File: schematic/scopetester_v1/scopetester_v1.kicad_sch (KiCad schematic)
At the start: 40 parts, among them J1 CON_PWR, J2 CON_OUT, J3 AVR_ISP, J4 CON_GND, SW1 SW_Push, U1 ATmega8A-P, Y1 12MHz

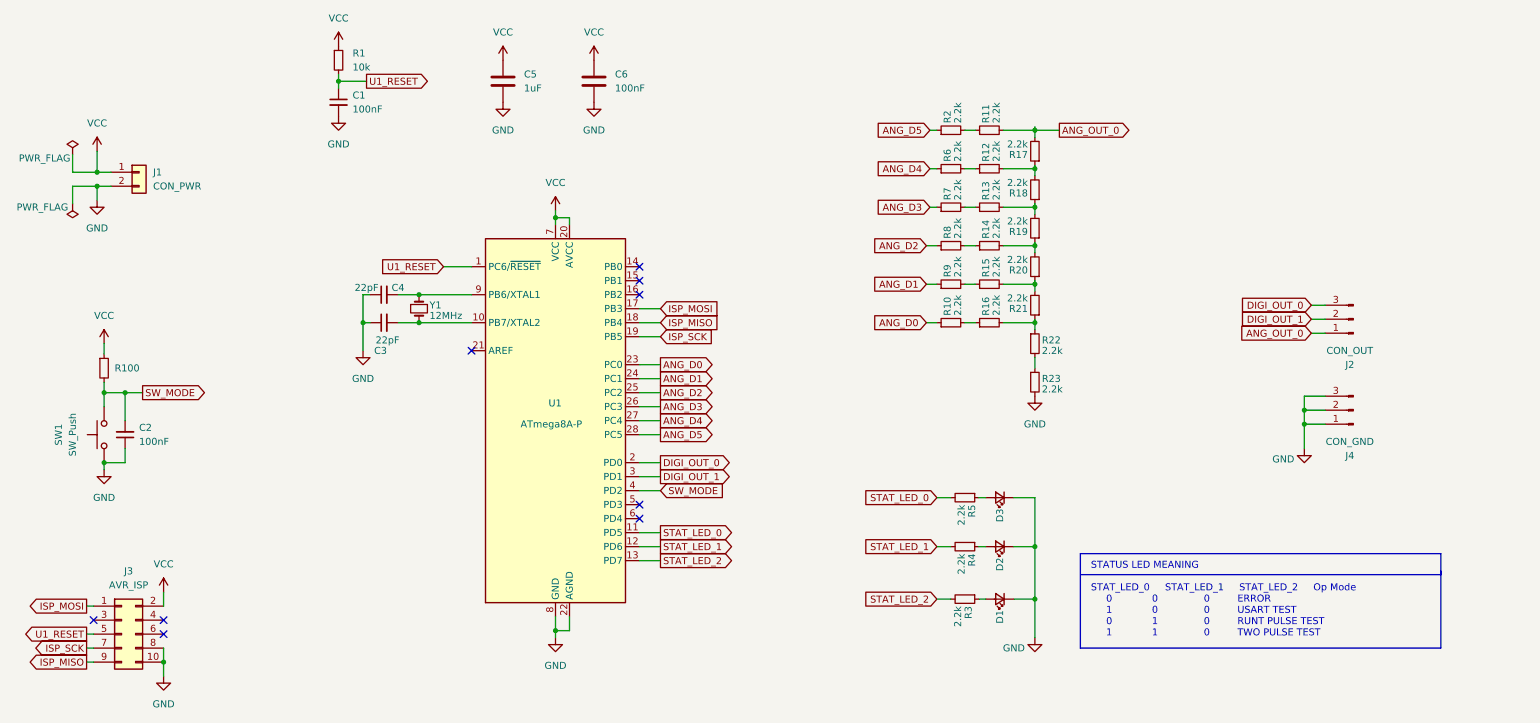
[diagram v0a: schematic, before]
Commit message: Minor updates, makes DAC clear & change of title
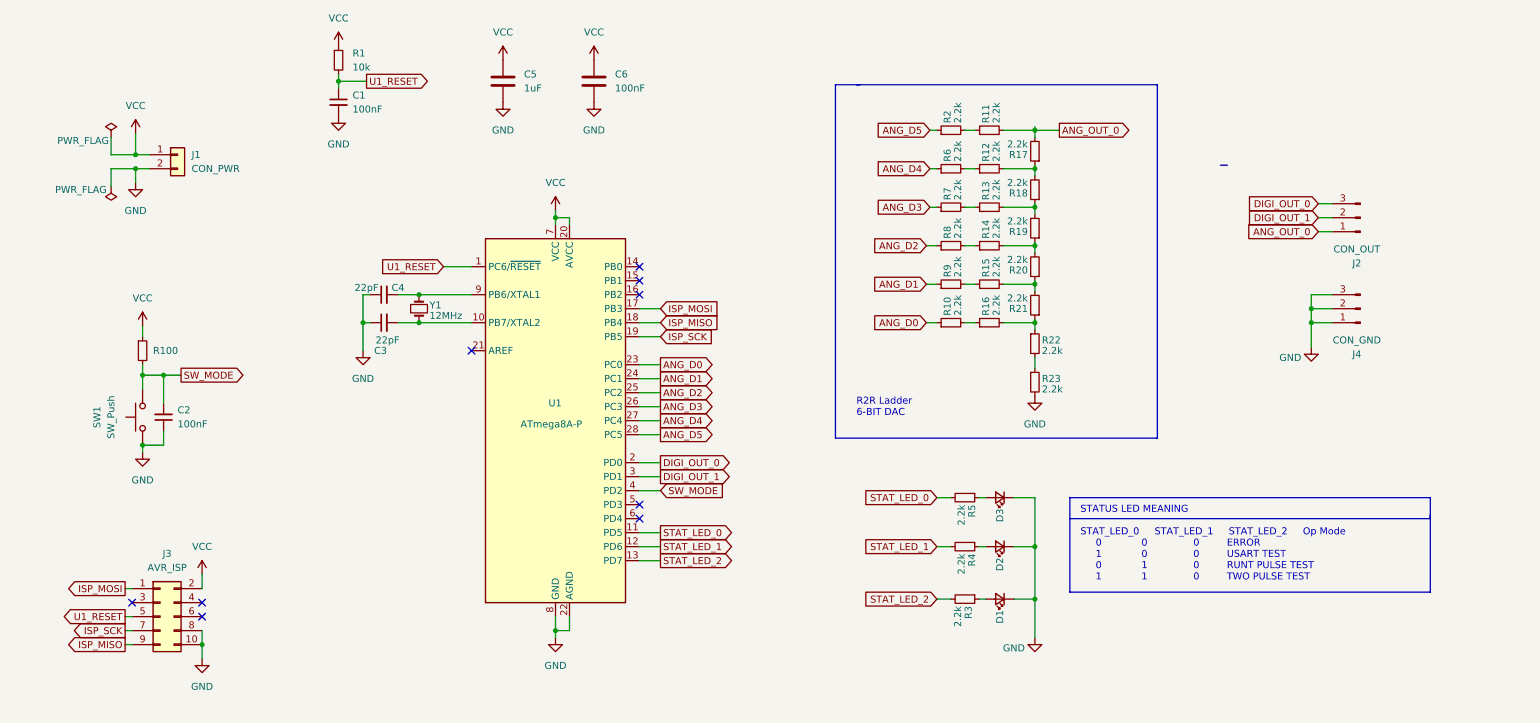
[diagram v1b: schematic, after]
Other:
- note added: "R2R Ladder 6-BIT DAC"
- moved on the sheet: C2, J1, J2, J3, J4, R100, SW1

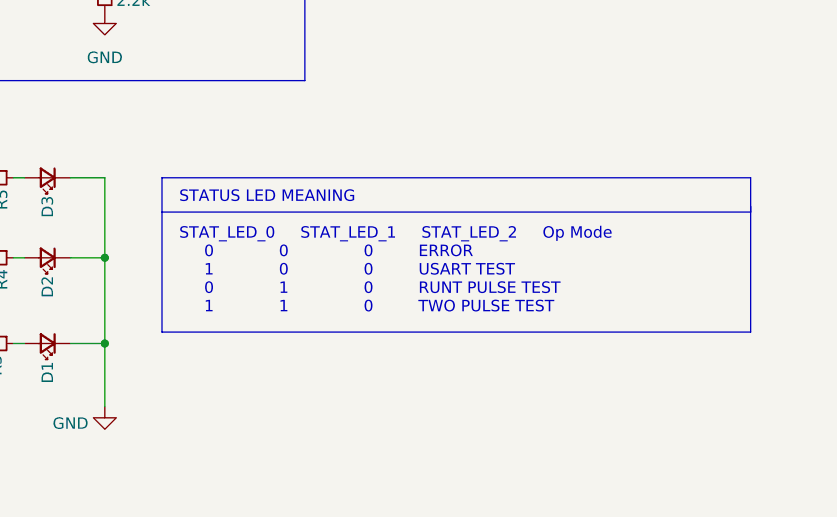
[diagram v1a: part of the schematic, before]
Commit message: Modes updated in schematic & initial PCB layout
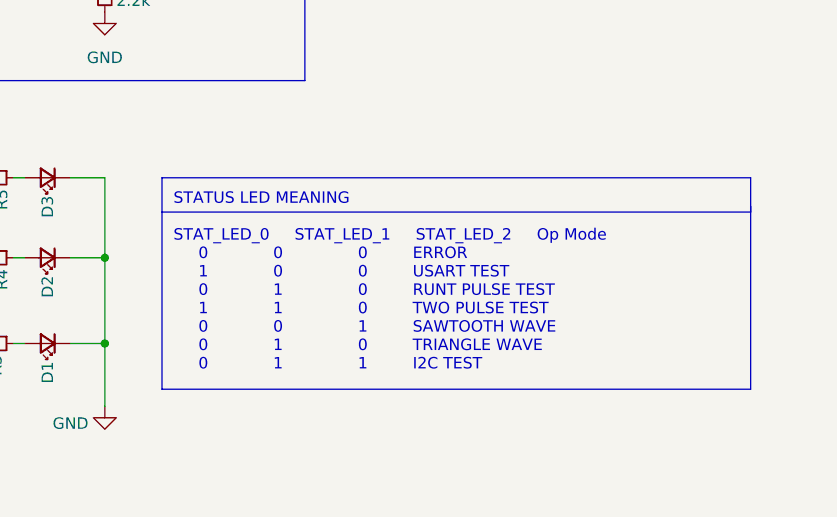
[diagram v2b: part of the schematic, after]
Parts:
- C1, C2, C3, C4, C6: footprint (none) -> Capacitor_THT:C_Disc_D3.4mm_W2.1mm_P2.50mm
- C5: footprint (none) -> Capacitor_THT:CP_Radial_D4.0mm_P1.50mm
- D1, D2, D3: footprint (none) -> LED_THT:LED_D3.0mm
- J1: footprint (none) -> Connector_PinHeader_1.00mm:PinHeader_1x02_P1.00mm_Vertical
- J2, J4: footprint (none) -> Connector_PinHeader_1.00mm:PinHeader_1x03_P1.00mm_Vertical
- J3: footprint (none) -> Connector_PinHeader_1.00mm:PinHeader_2x05_P1.00mm_Vertical
- R1, R10, R100, R11, R12, R13, R14, R15, R16, R17, R18, R19, R2, R20, R21, R22, R23, R3, R4, R5, R6, R7, R8, R9: footprint (none) -> Resistor_THT:R_Axial_DIN0411_L9.9mm_D3.6mm_P5.08mm_Vertical
- SW1: footprint (none) -> Button_Switch_THT:SW_PUSH_6mm_H5mm
- Y1: footprint (none) -> Crystal:Crystal_HC18-U_Vertical
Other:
- note added: "STATUS LED MEANING STAT_LED_0 STAT_LED_1 STAT_LED_2 Op Mode 0 0 0 ERROR 1 0 0 USART TEST 0 1 0 RUNT PULSE TEST 1 1 0 TWO PULSE TEST 0 0 1 SAWTOOTH WAVE 0 1 0 TRIANGLE WAVE 0 1 1 I2C TEST"
- note removed: "STATUS LED MEANING STAT_LED_0 STAT_LED_1 STAT_LED_2 Op Mode 0 0 0 ERROR 1 0 0 USART TEST 0 1 0 RUNT PULSE TEST 1 1 0 TWO PULSE TEST"

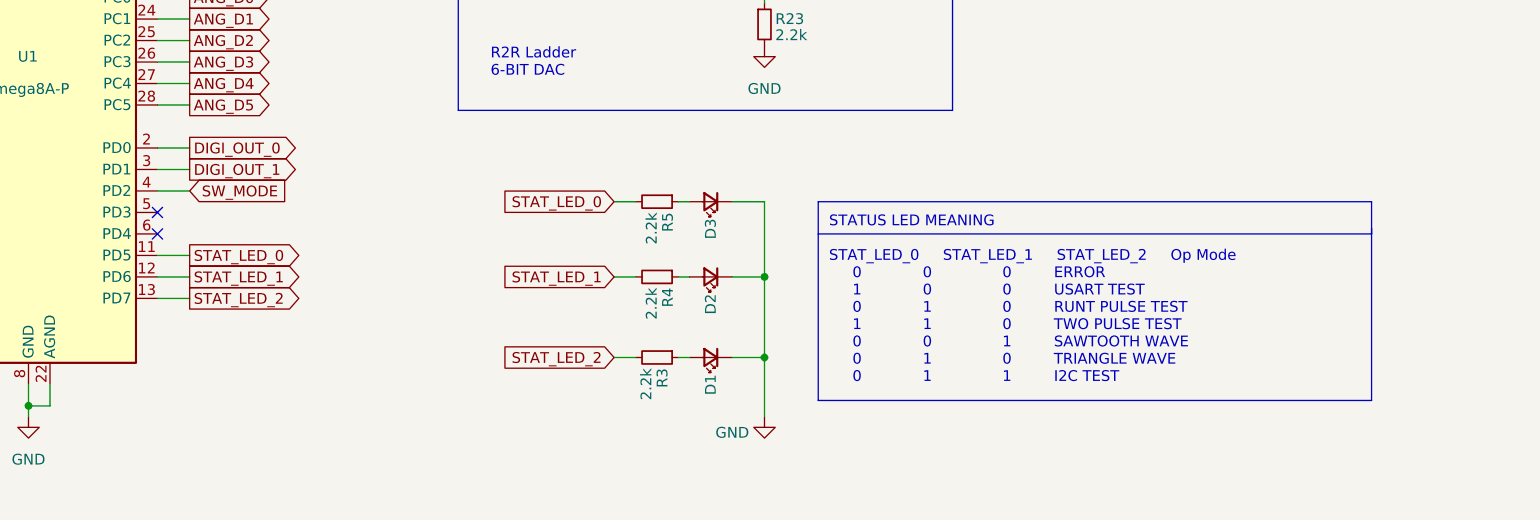
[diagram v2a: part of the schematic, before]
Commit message: There are now 4 status LEDs instead of 3
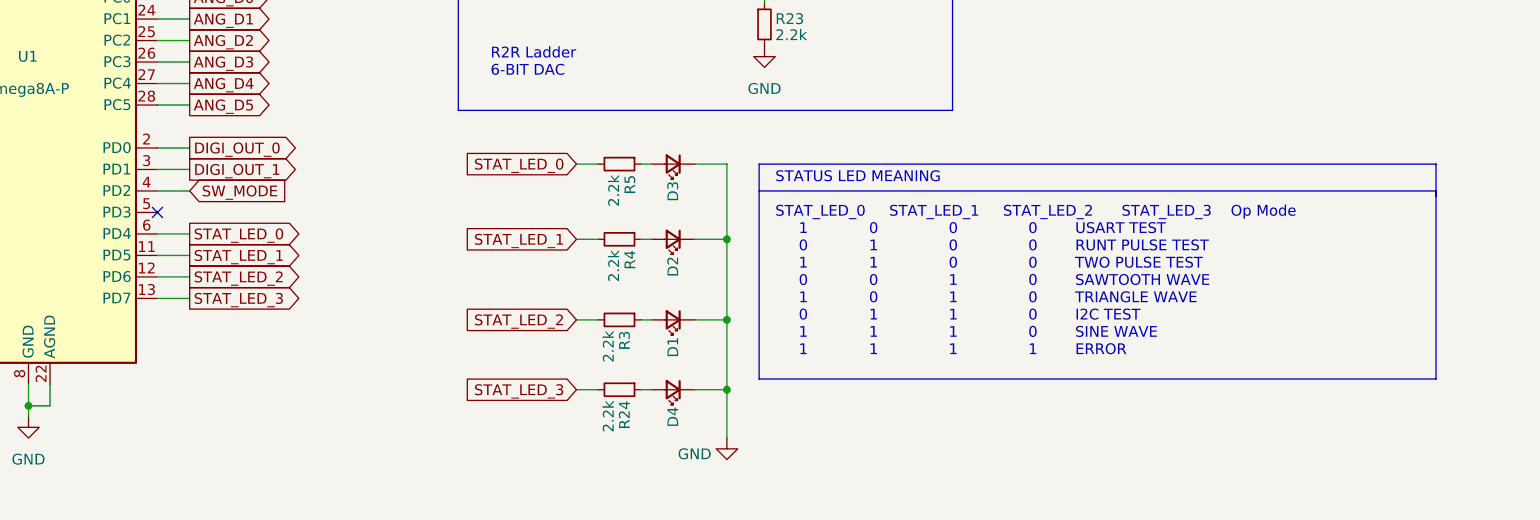
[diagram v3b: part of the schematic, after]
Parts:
- added D4: LED_Small, LED_THT:LED_D3.0mm, symbol Device:LED_Small
- added R24: 2.2k, Resistor_THT:R_Axial_DIN0411_L9.9mm_D3.6mm_P5.08mm_Vertical, symbol Device:R_Small
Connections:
- net GND: now also D4.1 (K)
- net STAT_LED_0: now also U1.6 (PD4); no longer U1.11 (PD5)
- net STAT_LED_1: now also U1.11 (PD5); no longer U1.12 (PD6)
- net STAT_LED_2: now also U1.12 (PD6); no longer U1.13 (PD7)
- new net: D4.2 (A), R24.1
- new net STAT_LED_3: R24.2, U1.13 (PD7)
- no-connect marks 9 -> 8
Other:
- note added: "STATUS LED MEANING STAT_LED_0 STAT_LED_1 STAT_LED_2 STAT_LED_3 Op Mode 1 0 0 0 USART TEST 0 1 0 0 RUNT PULSE TEST 1 1 0 0 TWO PULSE TEST 0 0 1 0 SAWTOOTH WAVE 1 0 1 0 TRIANGLE WAVE 0 1 1 0 I2C TEST 1 1 1 0 SINE WAVE 1 1 1 1 ERROR"
- note removed: "STATUS LED MEANING STAT_LED_0 STAT_LED_1 STAT_LED_2 Op Mode 0 0 0 ERROR 1 0 0 USART TEST 0 1 0 RUNT PULSE TEST 1 1 0 TWO PULSE TEST 0 0 1 SAWTOOTH WAVE 0 1 0 TRIANGLE WAVE 0 1 1 I2C TEST"
- moved on the sheet: D1, D2, D3, R3, R4, R5

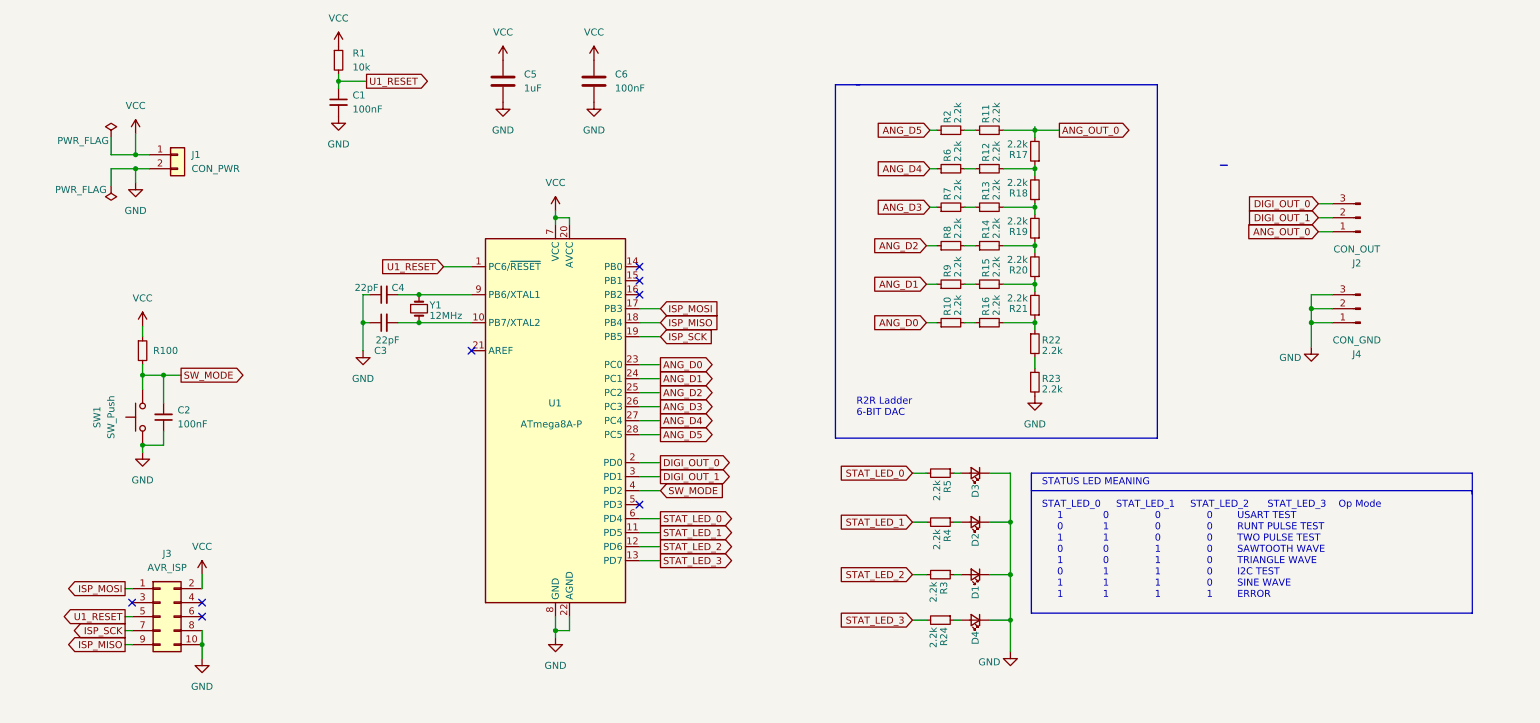
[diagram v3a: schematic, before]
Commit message: Replaced Vcc with +5V in schematic
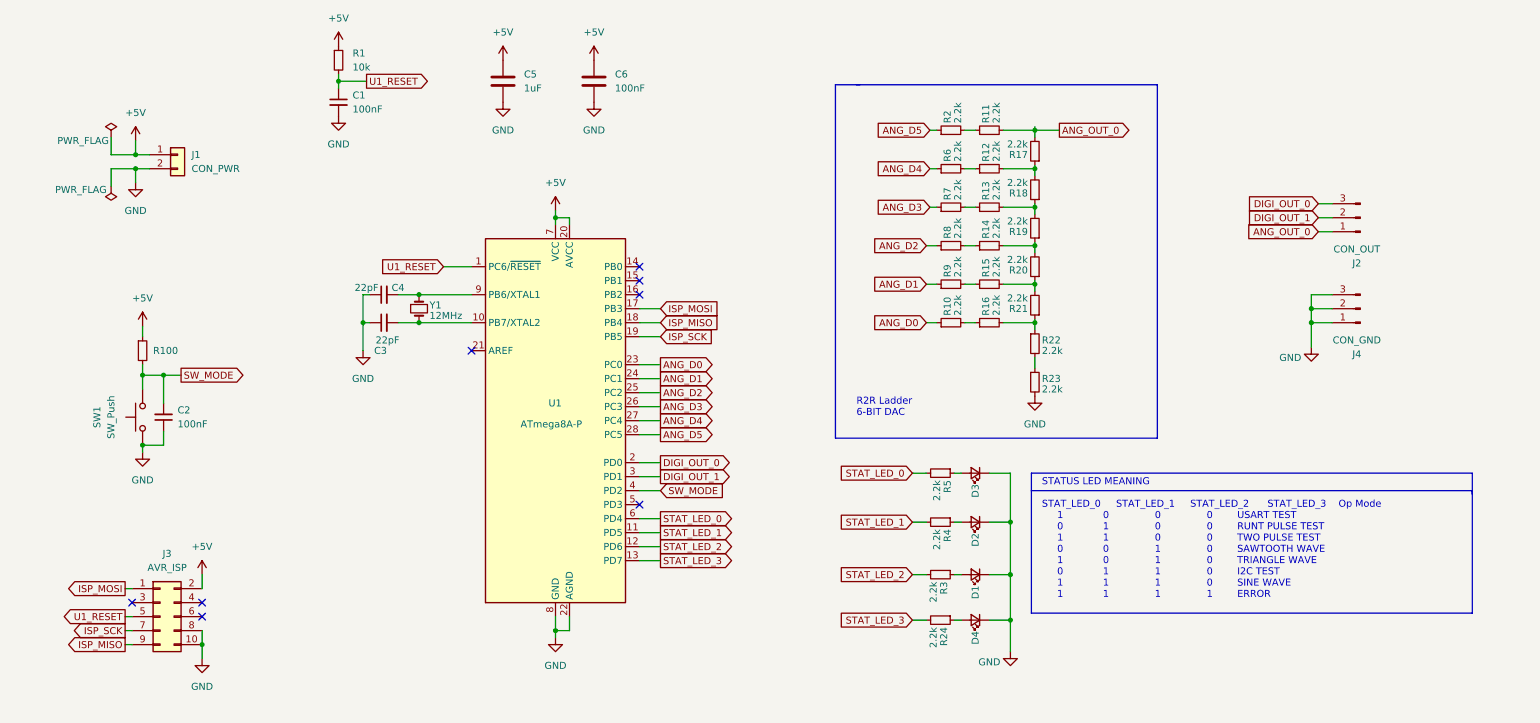
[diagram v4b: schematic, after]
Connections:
- net VCC renamed +5V

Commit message: Fix: More proper footprints instead of guessing
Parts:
- removed C5: 1uF, Capacitor_THT:CP_Radial_D4.0mm_P1.50mm, symbol Device:C
- removed J2: CON_OUT, Connector_PinHeader_1.00mm:PinHeader_1x03_P1.00mm_Vertical, symbol Connector:Conn_01x03_Male
- removed J4: CON_GND, Connector_PinHeader_1.00mm:PinHeader_1x03_P1.00mm_Vertical, symbol Connector:Conn_01x03_Male
- added C?: 1uF, Capacitor_THT:CP_Radial_D5.0mm_P2.50mm, symbol Device:C_Polarized
- added J2: Conn_01x04, Connector_PinHeader_2.54mm:PinHeader_1x04_P2.54mm_Vertical, symbol Connector_Generic:Conn_01x04
- C1, C2, C3, C4, C6: footprint Capacitor_THT:C_Disc_D3.4mm_W2.1mm_P2.50mm -> Capacitor_THT:C_Disc_D3.0mm_W1.6mm_P2.50mm
- J1: footprint Connector_PinHeader_1.00mm:PinHeader_1x02_P1.00mm_Vertical -> Connector_PinHeader_2.54mm:PinHeader_1x02_P2.54mm_Vertical
- J3: footprint Connector_PinHeader_1.00mm:PinHeader_2x05_P1.00mm_Vertical -> Connector_PinHeader_2.54mm:PinHeader_2x05_P2.54mm_Vertical
- R1, R10, R11, R12, R13, R14, R15, R16, R17, R18, R19, R2, R20, R21, R22, R23, R24, R3, R4, R5, R6, R7, R8, R9: footprint Resistor_THT:R_Axial_DIN0411_L9.9mm_D3.6mm_P5.08mm_Vertical -> Resistor_THT:R_Axial_DIN0207_L6.3mm_D2.5mm_P7.62mm_Horizontal
- SW1: footprint Button_Switch_THT:SW_PUSH_6mm_H5mm -> Button_Switch_THT:SW_PUSH_6mm_H4.3mm
- Y1: footprint Crystal:Crystal_HC18-U_Vertical -> Crystal:Crystal_HC49-4H_Vertical
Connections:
- net +5V: now also C?.1
- net ANG_OUT_0: now also J2.4 (Pin_4)
- net DIGI_OUT_0: now also J2.2 (Pin_2)
- net DIGI_OUT_1: now also J2.3 (Pin_3)
- net GND: now also C?.2, J2.1 (Pin_1)

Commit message: Initial commit for PCB layout
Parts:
- added C7: 100nF, Capacitor_THT:C_Disc_D3.0mm_W1.6mm_P2.50mm, symbol Device:C
- gave numbers to parts that had none: 1
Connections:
- net +5V: now also C7.1
- net GND: now also C7.2
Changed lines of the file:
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@@
+    (pin "2")
+  )
+  (symbol (lib_id "Device:C") (at 135.89 50.8 0) (unit 1)
+    (in_bom yes) (on_board yes) (fields_autoplaced)
+    (property "Reference" "C7" (id 0) (at 139.7 49.5299 0)
+      (effects (font (size 1.27 1.27)) (justify left))
+    )
+    (property "Value" "100nF" (id 1) (at 139.7 52.0699 0)
+      (effects (font (size 1.27 1.27)) (justify left))
+    )
+    (property "Footprint" "Capacitor_THT:C_Disc_D3.0mm_W1.6mm_P2.50mm" (id 2) (at 136.8552 54.61 0)
+      (effects (font (size 1.27 1.27)) hide)
+    )
+    (property "Datasheet" "~" (id 3) (at 135.89 50.8 0)
+      (effects (font (size 1.27 1.27)) hide)
+    )
+    (pin "1")
     (pin "2")
   )
@@
     (pin "2")
   )
+  (symbol (lib_id "power:GND") (at 135.89 54.61 0) (unit 1)
+    (in_bom yes) (on_board yes) (fields_autoplaced)
+    (property "Reference" "#PWR04" (id 0) (at 135.89 60.96 0)
+      (effects (font (size 1.27 1.27)) hide)
+    )
+    (property "Value" "GND" (id 1) (at 135.89 59.69 0))
+    (property "Footprint" "" (id 2) (at 135.89 54.61 0)
+      (effects (font (size 1.27 1.27)) hide)
+    )
+    (property "Datasheet" "" (id 3) (at 135.89 54.61 0)
+      (effects (font (size 1.27 1.27)) hide)
+    )
+    (pin "1")
+  )
   (symbol (lib_id "Device:R_Small") (at 186.055 66.675 90) (unit 1)
     (in_bom yes) (on_board yes)
@@
     (pin "1")
     (pin "2")
+  )
+  (symbol (lib_id "power:+5V") (at 135.89 46.99 0) (unit 1)
+    (in_bom yes) (on_board yes) (fields_autoplaced)
+    (property "Reference" "#PWR03" (id 0) (at 135.89 50.8 0)
+      (effects (font (size 1.27 1.27)) hide)
+    )
+    (property "Value" "+5V" (id 1) (at 135.89 41.91 0))
+    (property "Footprint" "" (id 2) (at 135.89 46.99 0)
+      (effects (font (size 1.27 1.27)) hide)
+    )
+    (property "Datasheet" "" (id 3) (at 135.89 46.99 0)
+      (effects (font (size 1.27 1.27)) hide)
+    )
+    (pin "1")
   )
   (symbol (lib_id "Device:R_Small") (at 193.04 94.615 90) (unit 1)
@@
   (symbol (lib_id "Device:R_Small") (at 39.37 99.695 0) (unit 1)
     (in_bom no) (on_board no)
-    (property "Reference" "R100" (id 0) (at 41.275 99.695 0)
+    (property "Reference" "R100" (id 0) (at 40.64 98.425 0)
       (effects (font (size 1.27 1.27)) (justify left))
     )
     (property "Value" "2.2k" (id 1) (at 40.64 100.33 0)
-      (effects (font (size 1.27 1.27)) (justify left) hide)
+      (effects (font (size 1.27 1.27)) (justify left))
     )
     (property "Footprint" "Resistor_THT:R_Axial_DIN0411_L9.9mm_D3.6mm_P5.08mm_Vertical" (id 2) (at 39.37 99.695 0)
@@
   (symbol (lib_id "Device:C_Polarized") (at 107.95 50.8 0) (unit 1)
     (in_bom yes) (on_board yes) (fields_autoplaced)
-    (property "Reference" "C?" (id 0) (at 111.76 48.6409 0)
+    (property "Reference" "C5" (id 0) (at 111.76 48.6409 0)
       (effects (font (size 1.27 1.27)) (justify left))
     )
@@
       (reference "#PWR02") (unit 1) (value "GND") (footprint "")
     )
+    (path "/4b742071-f275-4692-a661-01039e3a5e5f"
+      (reference "#PWR03") (unit 1) (value "+5V") (footprint "")
+    )
+    (path "/1c178f09-07c2-40f5-9942-b5c697722e4f"
+      (reference "#PWR04") (unit 1) (value "GND") (footprint "")
+    )
     (path "/a95e1ba5-6a40-4ce3-b0d2-eba402d6e730"
       (reference "#PWR0101") (unit 1) (value "GND") (footprint "")
@@
       (reference "C4") (unit 1) (value "22pF") (footprint "Capacitor_THT:C_Disc_D3.0mm_W1.6mm_P2.50mm")
     )
+    (path "/9c053abc-01c1-4f7c-a730-ee7009b7e805"
+      (reference "C5") (unit 1) (value "1uF") (footprint "Capacitor_THT:CP_Radial_D5.0mm_P2.50mm")
+    )
     (path "/9dd78695-86eb-4298-a658-1c210fd99dfc"
       (reference "C6") (unit 1) (value "100nF") (footprint "Capacitor_THT:C_Disc_D3.0mm_W1.6mm_P2.50mm")
     )
-    (path "/9c053abc-01c1-4f7c-a730-ee7009b7e805"
-      (reference "C?") (unit 1) (value "1uF") (footprint "Capacitor_THT:CP_Radial_D5.0mm_P2.50mm")
+    (path "/0d045e26-6c0b-4bbe-ab02-697106284228"
+      (reference "C7") (unit 1) (value "100nF") (footprint "Capacitor_THT:C_Disc_D3.0mm_W1.6mm_P2.50mm")
     )
     (path "/caff683e-4ee6-4902-a455-aba0f4249ba5"
